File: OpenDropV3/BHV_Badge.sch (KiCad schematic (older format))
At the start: 259 parts, among them J1 USB_C_Receptacle, J2 Conn_02x05_Odd_Even, P1 CONN_01X01, P10 CONN_01X01, P11 CONN_01X01, P12 CONN_01X01, P13 ScrewPad1, P14 ScrewPad2, P15 ScrewPad3, P16 ScrewPad4, P2 ScrewPad4, P3 CONN_01X01, P4 CONN_PSEUDO_AC, P7 CONN_01X01, P8 CONN_01X01, P9 CONN_01X01, SW1 SW_PUSH, SW2 SW_PUSH, SW3 PTS810_SJK_250_SMTR_LFS, SW5 SPST, T1 TK560P60Y, U1 MAX1771ESA, U10 AQY210EH, U11 AQY210EH, U12 AQY210EH, U13 AQY210EH, U14 TLV1117-33, U15 MCP41010, U16 74xx14, U2 HV507, U3 PAM8301, U4 HV507, U5 SAMD21G18B-A changed from SAM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, U6 MCP6002, U7 HCPL0534, U8 HCPL0534, U9 HCPL0534, Y1 32.765

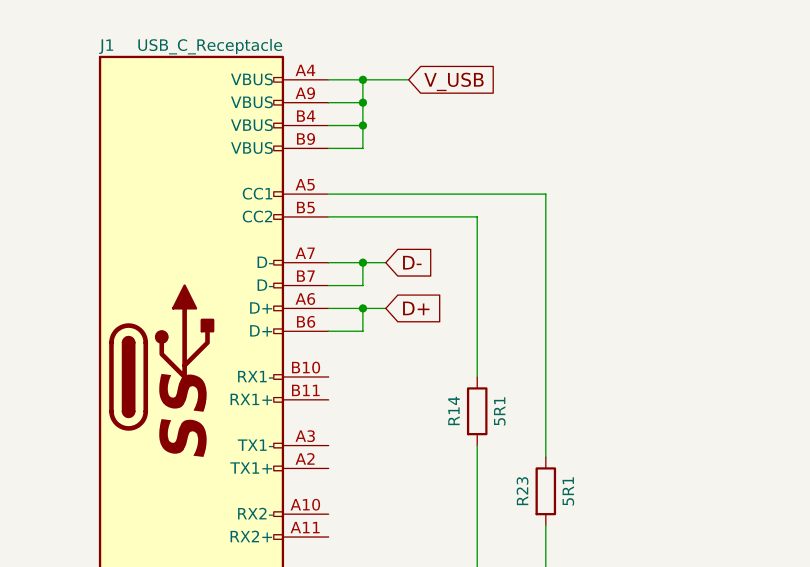
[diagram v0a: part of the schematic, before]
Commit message: Updated footprints and adjusted copper pour areas
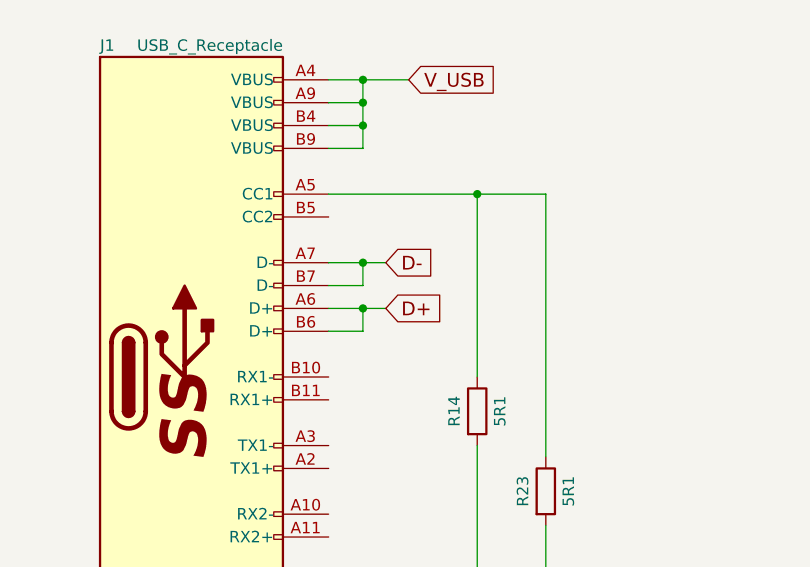
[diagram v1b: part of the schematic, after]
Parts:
- R14, R23: footprint Resistors_SMD:R_0805 -> GaudiLabsFootPrints:R_0805_HeatPad
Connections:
- net at J1.A5 (CC1), R23.1: now also R14.1
- net at J1.B5 (CC2): no longer R14.1
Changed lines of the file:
@@
 F 0 "R14" V 21400 12900 50  0000 C CNN
 F 1 "5R1" V 21600 12900 50  0000 C CNN
-F 2 "Resistors_SMD:R_0805" V 21430 12900 30  0001 C CNN
+F 2 "GaudiLabsFootPrints:R_0805_HeatPad" V 21430 12900 30  0001 C CNN
 F 3 "" H 21500 12900 30  0000 C CNN
 	1    21500 12900
@@
 F 0 "R23" V 21700 13250 50  0000 C CNN
 F 1 "5R1" V 21900 13250 50  0000 C CNN
-F 2 "Resistors_SMD:R_0805" V 21730 13250 30  0001 C CNN
+F 2 "GaudiLabsFootPrints:R_0805_HeatPad" V 21730 13250 30  0001 C CNN
 F 3 "" H 21800 13250 30  0000 C CNN
 	1    21800 13250
@@
 $EndComp
 Wire Wire Line
+	20850 11950 21800 11950
+Wire Wire Line
 	21800 11950 21800 13100
+Wire Wire Line
+	21500 12750 21500 11950
+Connection ~ 21500 11950
 Wire Wire Line
 	21800 14450 21800 13400
@@
 	12350 13250 12500 13250
 Connection ~ 12500 13350
-Wire Wire Line
-	20850 11950 21800 11950
-Wire Wire Line
-	20850 12050 21500 12050
-Wire Wire Line
-	21500 12050 21500 12750
 $EndSCHEMATC
